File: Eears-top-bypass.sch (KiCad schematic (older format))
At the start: 125 parts, among them J3 Conn_01x02

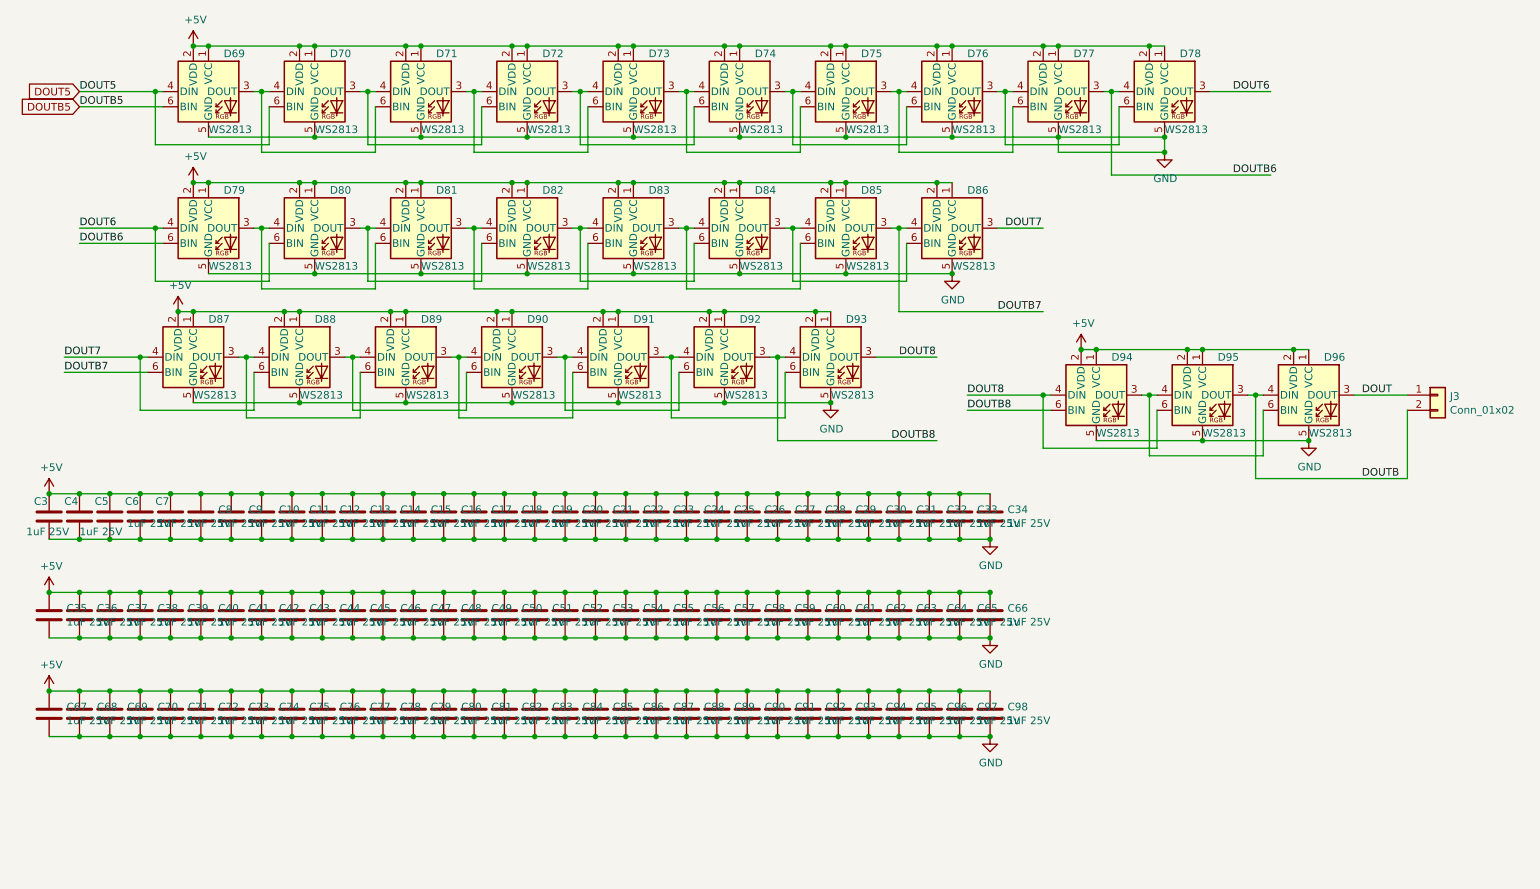
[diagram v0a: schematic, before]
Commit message: Added more ESD protection and moved a few components.
Version 2.0

Signed-off-by: Aaron Williams <aaron.w2@gmail.com>
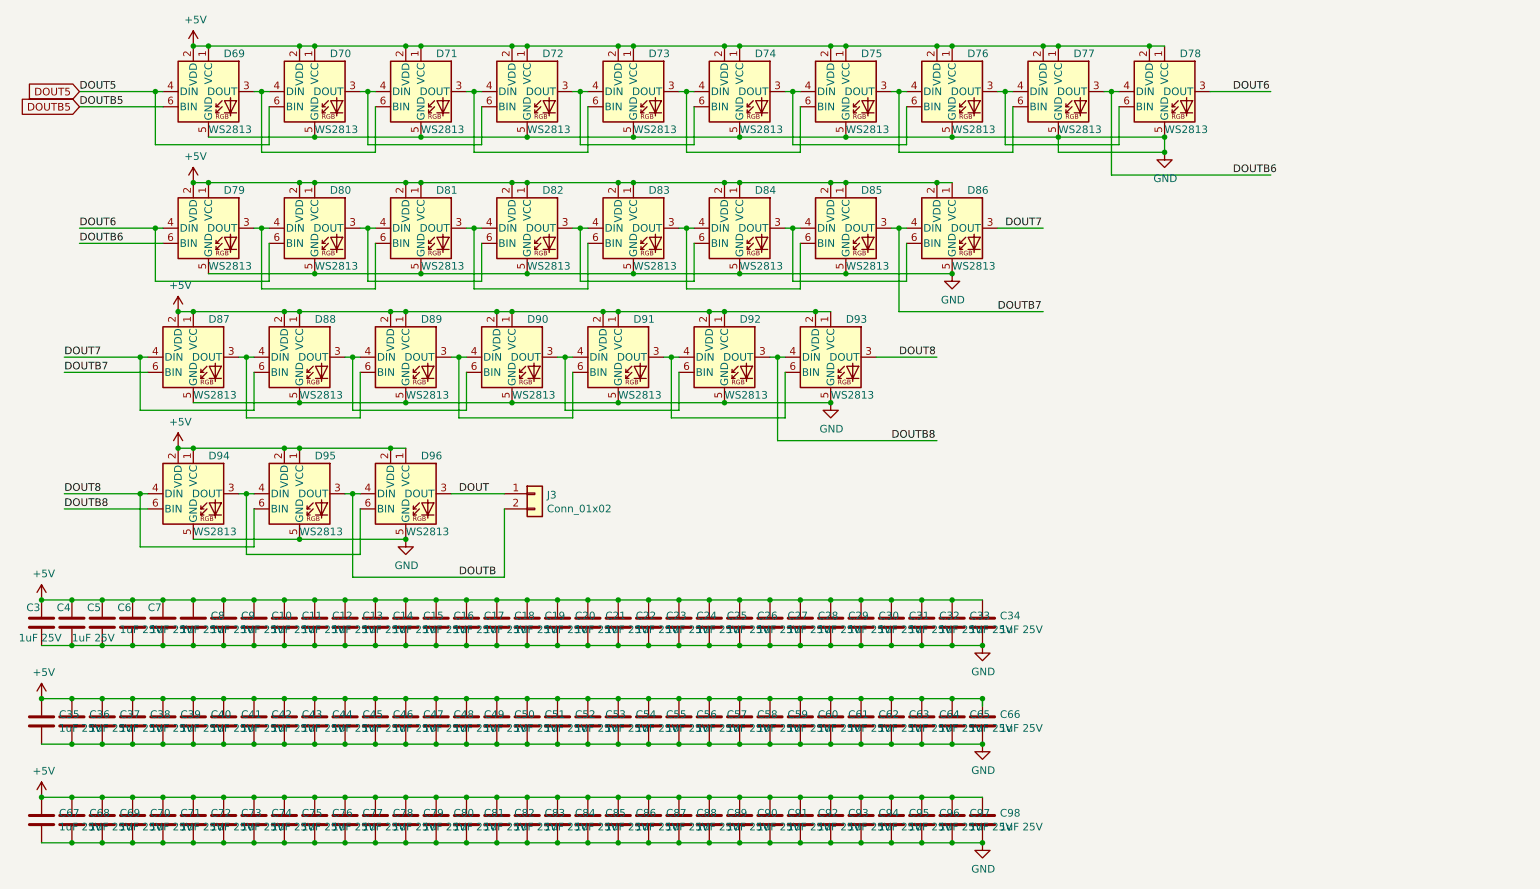
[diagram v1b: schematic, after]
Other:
- moved on the sheet: C10, C11, C12, C13, C14, C15, C16, C17, C18, C19, C20, C21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
